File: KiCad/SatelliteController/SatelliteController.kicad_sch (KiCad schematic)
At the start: 32 parts, among them J1 CONN_ICSP, J2 CONN_USB, J3 USB_B_Micro, U1 FT232RL, U2 ATMEGA2560-16AUR, Y1 HUSG-16.000-20

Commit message: N2O圧力計測回路を追加
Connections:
- net VREF_N2O_PRESS: now also U2.87 (PK2)
- no-connect marks 43 -> 42
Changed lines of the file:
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@@
   (no_connect (at 54.61 129.54))
   (no_connect (at 95.25 170.18))
-  (no_connect (at 54.61 99.06))
   (no_connect (at 95.25 180.34))
   (no_connect (at 199.39 53.34))
@@
     (stroke (width 0) (type default))
   )
+  (wire (pts (xy 52.07 99.06) (xy 54.61 99.06))
+    (stroke (width 0) (type default))
+  )
   (wire (pts (xy 77.47 40.64) (xy 129.54 40.64))
     (stroke (width 0) (type default))
@@
     )
   )
-  (global_label "VREF_N2O_PRESS" (shape input) (at 105.41 165.1 0) (fields_autoplaced)
-    (effects (font (size 1.27 1.27)) (justify left))
-    (property "Intersheetrefs" "${INTERSHEET_REFS}" (at 124.8257 165.1 0)
-      (effects (font (size 1.27 1.27)) (justify left) hide)
-    )
-  )
+  (global_label "VREF_N2O_PRESS" (shape input) (at 52.07 99.06 180) (fields_autoplaced)
+    (effects (font (size 1.27 1.27)) (justify right))
+    (property "Intersheetrefs" "${INTERSHEET_REFS}" (at 32.6543 99.06 0)
+      (effects (font (size 1.27 1.27)) (justify right) hide)
+    )
+  )

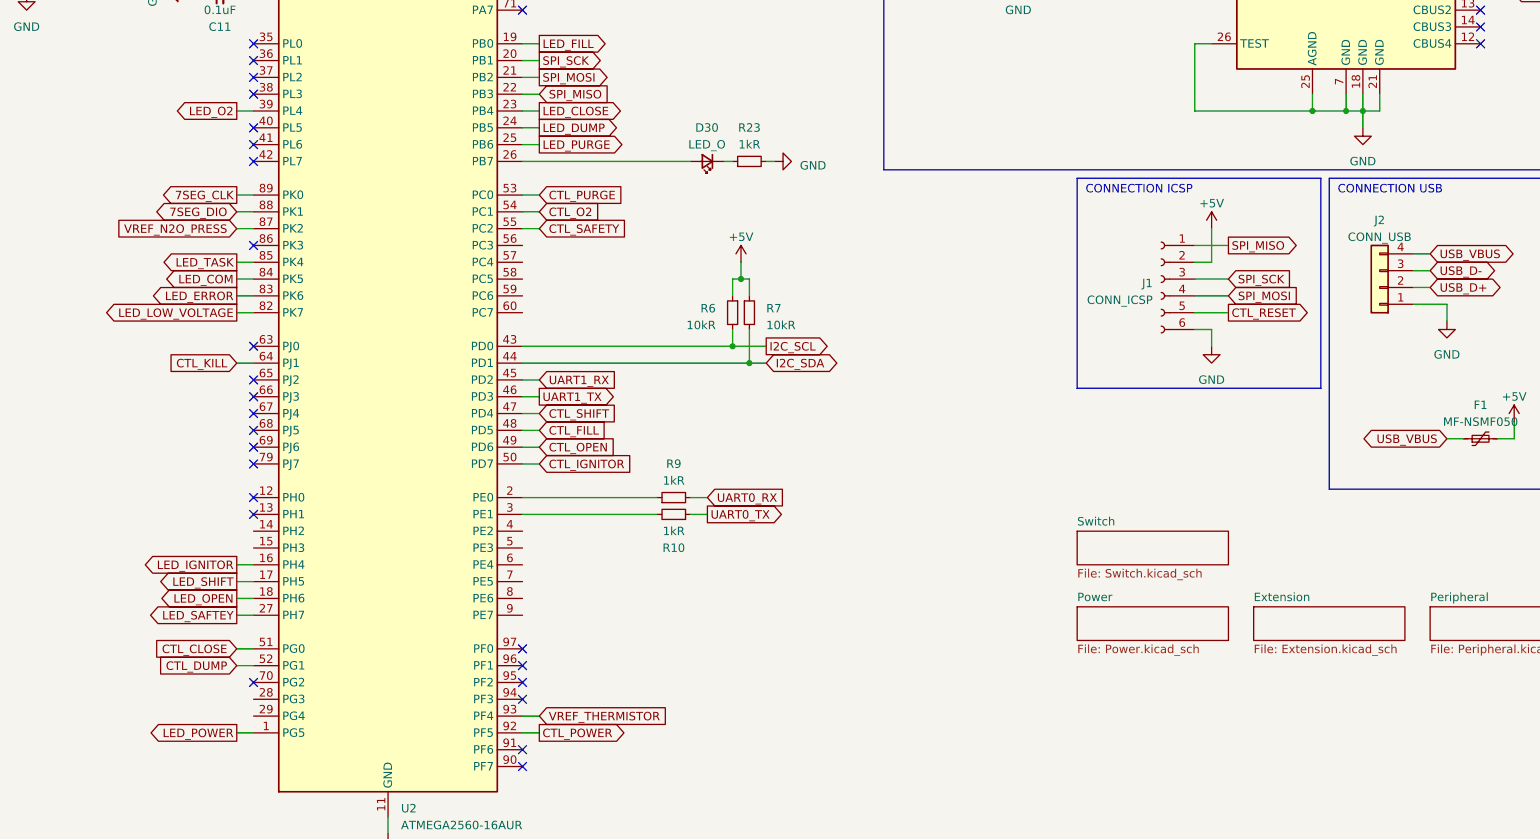
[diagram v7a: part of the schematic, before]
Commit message: サテコンのボード図を作成
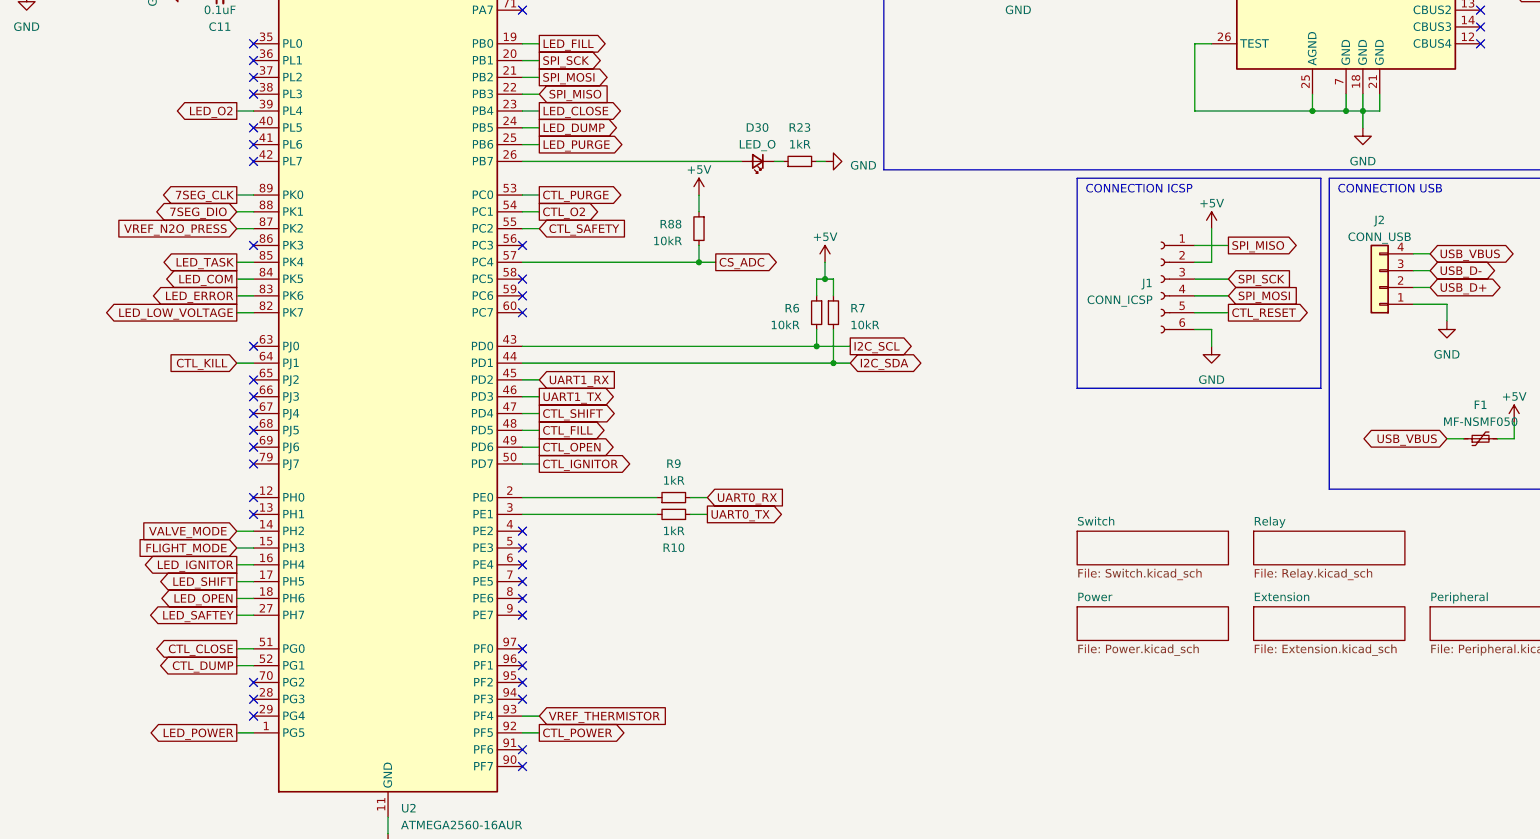
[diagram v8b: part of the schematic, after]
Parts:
- added R88: 10kR, Resistor_SMD:R_0603_1608Metric_Pad0.98x0.95mm_HandSolder, symbol Device:R_Small
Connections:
- net +5V: now also R88.1
- net VALVE_MODE: now reaches U2.14 (PH2)
- net FLIGHT_MODE: now reaches U2.15 (PH3)
- net CS_ADC: now reaches U2.57 (PC4)
- net CS_ADC: now also R88.2
- no-connect marks 42 -> 54
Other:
- added sheet Relay (Relay.kicad_sch)
- moved on the sheet: D30, R23, R6, R7
